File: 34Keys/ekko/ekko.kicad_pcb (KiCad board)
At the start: 2 copper layers, 108.8 x 91.3 mm, 27 parts, among them SW10 SW_PUSH, SW11 SW_PUSH, SW12 SW_PUSH, SW14 SW_PUSH, SW15 SW_PUSH, SW16 SW_PUSH, SW17 SW_PUSH, SW18 SW_PUSH, SW2 SW_PUSH, SW20 SW_PUSH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

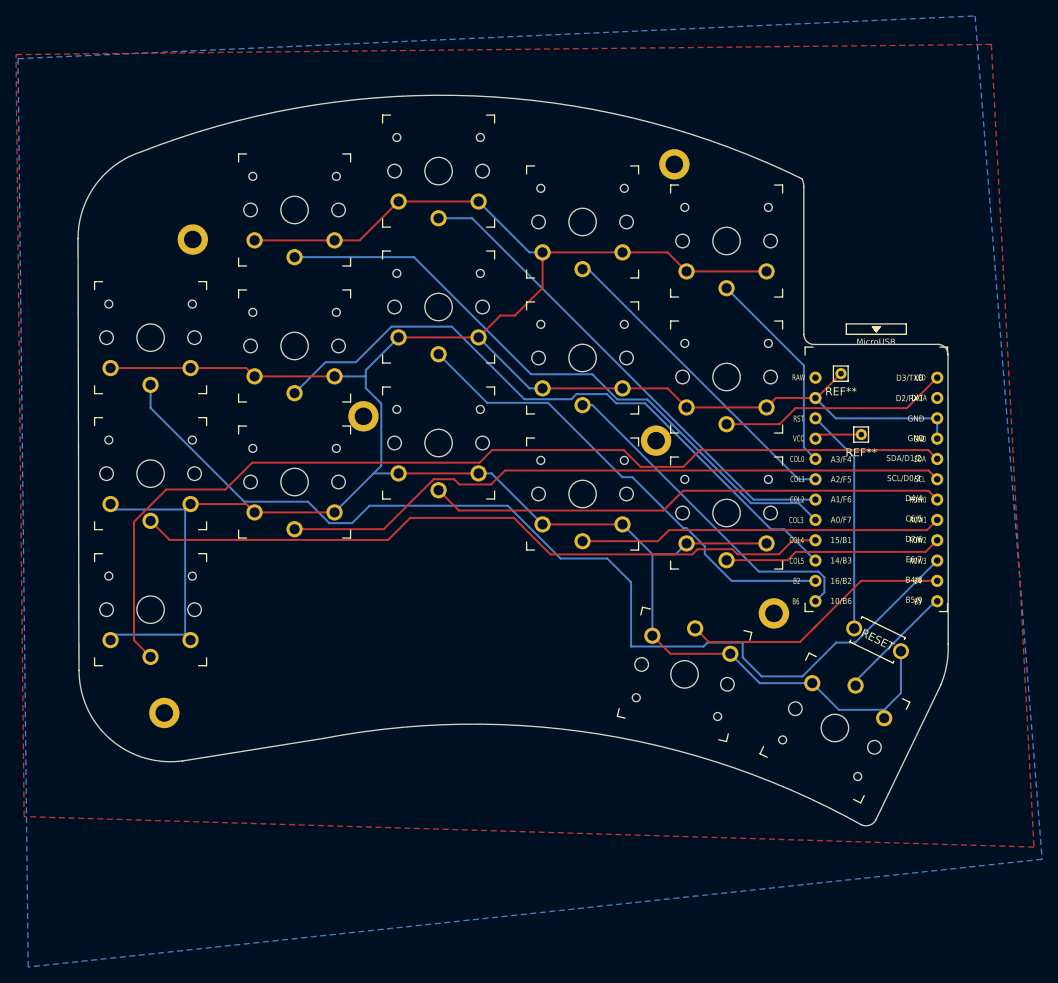
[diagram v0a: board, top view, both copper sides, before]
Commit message: 36-key version of the Ekko
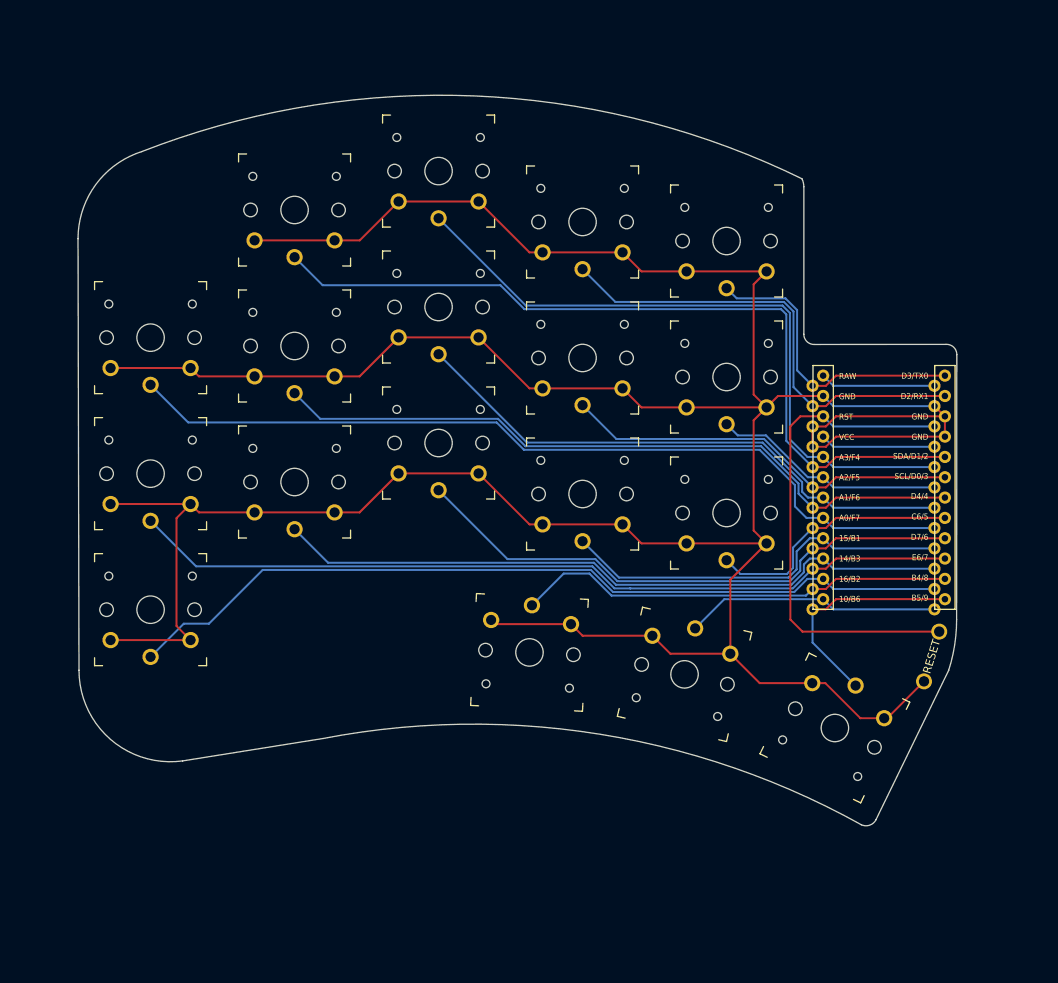
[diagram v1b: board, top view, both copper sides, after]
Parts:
- removed REF** (x2): Pin_D0.7mm_L6.5mm_W1.8mm_FlatFork, Connector_Pin:Pin_D0.7mm_L6.5mm_W1.8mm_FlatFork
- removed Ref** (x6): Val**, MountingHole:MountingHole_2.2mm_M2_DIN965_Pad
- added ?: , , F.Cu at (-3.17, -14.6)
- added ?: , , F.Cu at (-3.17, -17.1)
- added ?: , , F.Cu at (-3.17, -19.7)
- added ?: , , F.Cu at (-3.17, -21.6)
- added ?: , , F.Cu at (-5.71, -19.7)
- added SW20: SW_PUSH, chocs:SW_PG1350_reversible_b2, B.Cu at (91.4, 82.3)
- U1: footprint kbd:ProMicro_v3 -> kbd:ProMicro_v2
- moved RSW1 7.07 mm to (141.6, 82.9), turned to 253 degrees
- moved U1 0.95 mm to (135.6, 62.2)
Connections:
- RSW1 pad 1: reset -> GND
- RSW1 pad 2: GND -> reset
- SW10 pad 1: Net-(U1-Pad14) -> col2
- SW11 pad 1: Net-(U1-Pad13) -> SCL
- SW12 pad 1: LED -> col1
- SW14 pad 1: SDA -> Net-(U1-Pad14)
- SW15 pad 1: SCL -> col5
- SW16 pad 1: row0 -> row2
- SW17 pad 1: row1 -> col4
- SW18 pad 1: row2 -> row1
- SW2 pad 1: row3 -> col3
- SW20 pad 1: Net-(U1-Pad11) -> Net-(U1-Pad13)
- SW3 pad 1: col3 -> SDA
- SW4 pad 1: col2 -> Net-(D20-Pad2)
- SW5 pad 1: col1 -> data
- SW6 pad 1: Net-(D20-Pad2) -> LED
- SW8 pad 1: col4 -> row3
- SW9 pad 1: col5 -> row0
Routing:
- net GND: track 384.6 -> 450.9 mm
- net data: track 0.00 -> 58.4 mm
- net Net-(D20-Pad2): track 25.9 -> 84.1 mm
- net Net-(U1-Pad14): track 59.4 -> 105.0 mm
- net row2: track 27.4 -> 71.0 mm
- net col4: track 88.4 -> 49.7 mm
- net SCL: track 84.4 -> 50.1 mm
- net reset: track 28.3 -> 62.5 mm
- net col3: track 78.7 -> 107.0 mm
- net row3: track 129.1 -> 104.3 mm
- net row0: track 64.9 -> 88.5 mm
- net SDA: track 124.1 -> 101.9 mm
- net Net-(U1-Pad11): track 34.6 -> 55.3 mm
- net Net-(U1-Pad24): track 0.00 -> 14.4 mm
- net Net-(U1-Pad12): track 14.9 -> 28.8 mm
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- removed copper zone on B.Cu, net (none)
- removed copper zone on F.Cu, net (none)
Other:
- board size 108.8 x 91.3 mm -> 109.8 x 91.3 mm
